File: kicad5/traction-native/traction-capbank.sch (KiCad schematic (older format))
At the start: 26 parts

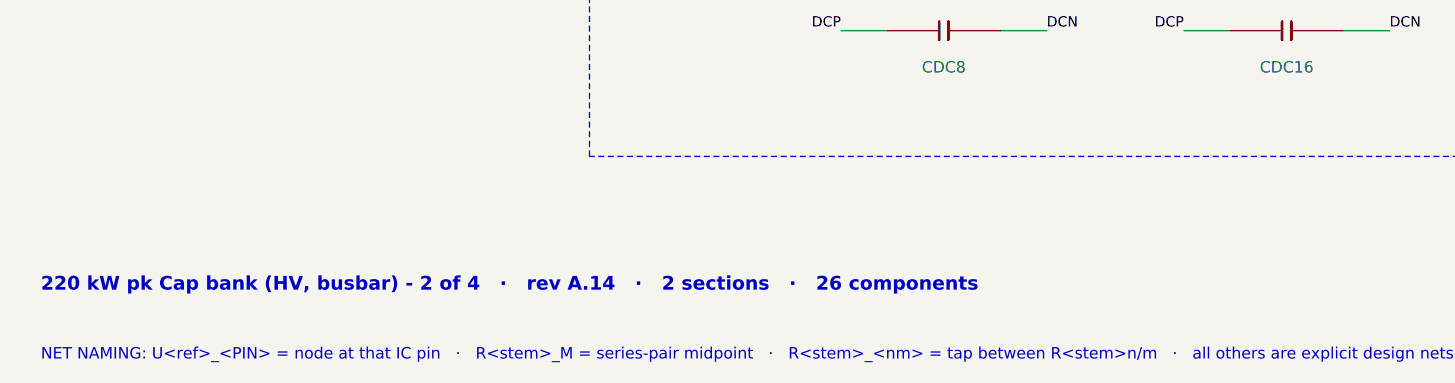
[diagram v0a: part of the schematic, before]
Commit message: Rev A.16: round 17 — gap closure (F174-F189) + round 16 rev A.15 (F167-F173): every gap closed, upgraded or numbered
Round 16 (rev A.15, three rechecks of 32214be): exciter MFB gain 24 k -> 28 k with the amplitude
planes (setpoint 7.2 V pp at the monitor), unidirectional exciter TVS, /33X hold 0.07 A, firmware
acquisition contracts (phase triplets, resolver frame age, coherent SDADC frames); BOM furnished
(spec-class capacitors, drawn-size gate in bom-gen, last placeholders bound with archived sheets).

Round 17 (rev A.16, "close all gaps" / "feel free to upgrade"):
- Hardware: DEXP/DEXN PMEG4050EP-Q rated back-drive diversion (closes the ALM2402 OPEN row);
  exciter TVS -> SMDJ8.5A-HRA (3 kW, AEC-Q101, same pad); fault rows split single fault (PASS
  at any source impedance) vs load-dump-coincident double event; LV entry re-designed as
  LET-THROUGH for ISO 16750-2 test B (TPSMC33A-VR/TPSMC18A-VR anti-series pair at the pin ahead
  of the reverse Schottky, TPSMC33CA-VR on the power board, CLVC3 100 uF hybrid polymer, FLVC
  5 A fuse, DIGN US1M, ULDO15 D2PAK) — pulse 1 was avalanching DREVC, the 2023 26 V jump start
  opened the old TVS, the polyfuse was undersized at 9 V; RFS4 -> ESR18 1206.
- Stale/unsourced rows recomputed: cold-crank excitation, PTC hold (IR-13), discharge resistor
  no-flame statement, hall reference drift, ASC command-path collapse.
- KiCad: a KiCad 9/10 set (kicad/traction, Traction-Inverter-KiCad-modern.zip) proved by
  kicad-cli netlist export on every board with mutation tests; KiCad 10 cannot resolve the KiCad 5
  legacy symbols; the proof exposed harness pins numbered P1-P40 and the SMDJ drawn as a resistor
  in the legacy generator — fixed; sym-lib-table + cache library in both legacy sets.
- Firmware: all 35 open contract items closed (FW-08 zero-current decision, FW-31 liveness,
  FW-32 UDS service-lock routine, FW-33 supply-overvoltage supervision), FS26 watchdog answer
  3.0 ms -> 2.0 ms, ASC-exit release wait CAL, 39-row silicon/RM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
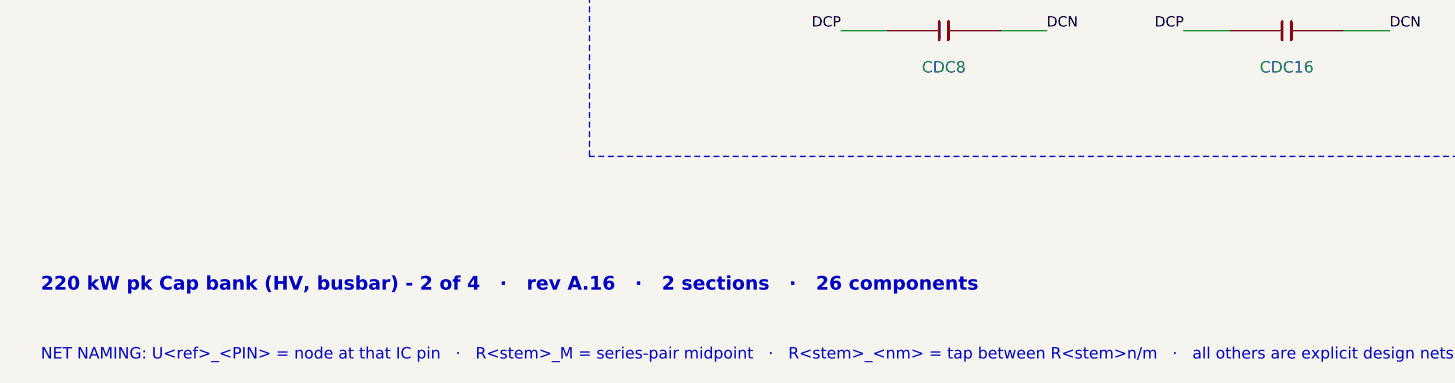
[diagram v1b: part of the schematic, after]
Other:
- note added: "220 kW pk Cap bank (HV, busbar) - 2 of 4 · rev A.16 · 2 sections · 26 components"
- note removed: "220 kW pk Cap bank (HV, busbar) - 2 of 4 · rev A.14 · 2 sections · 26 components"
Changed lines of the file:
@@
 Title "Traction Inverter — Cap bank (busbar assembly, 320 uF)"
 Date "2026-09-23"
-Rev "A.14"
+Rev "A.16"
 Comp "Traction Inverter 220 kW pk - Cap bank (HV, busbar), sheet 2 of 4"
 Comment1 "Inverter = Power board + Cap bank busbar + bolt-on Discharge board (all HV) + Control card (LV); safe state holds with any link lost"
@@
 $EndDescr
 Text Notes 600 5100 0    60   ~ 12
-220 kW pk Cap bank (HV, busbar) - 2 of 4   ·   rev A.14   ·   2 sections   ·   26 components
+220 kW pk Cap bank (HV, busbar) - 2 of 4   ·   rev A.16   ·   2 sections   ·   26 components
 Text Notes 600 5400 0    50   ~ 0
 NET NAMING: U<ref>_<PIN> = node at that IC pin   ·   R<stem>_M = series-pair midpoint   ·   R<stem>_<nm> = tap between R<stem>n/m   ·   all others are explicit design nets   ·   same name on another sheet = same net, joined only at the named connector/stud/tab

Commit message: Rev A.17: round 18 — three rechecks of 4425af9 (F190-F198): diversion diodes on the amplifier node (loop passes RSX), diode cell cathode = pin 1 on all 35 diodes, exciter TVS/PTC rows at worst corners + ECU-asleep sustained short (WARN rows, layout rule, QP-RX-04 2b gate), anti-surge RSX, NCV4276C reverse current = QP-RX-05 gate + VR-33, IR-16/IR-42, firmware FW-34..36 (sample freshness, cadence-locked resolver frames, latency sign) + three self-found instances
Co-Authored-By: Claude Fable 5.1 <noreply@anthropic.com>
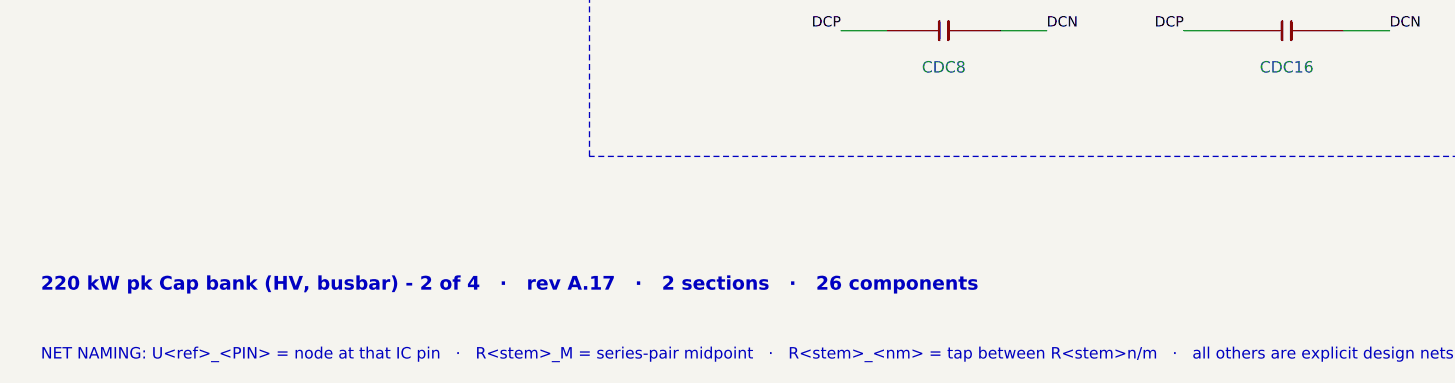
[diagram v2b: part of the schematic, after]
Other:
- note added: "220 kW pk Cap bank (HV, busbar) - 2 of 4 · rev A.17 · 2 sections · 26 components"
- note removed: "220 kW pk Cap bank (HV, busbar) - 2 of 4 · rev A.16 · 2 sections · 26 components"
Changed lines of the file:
@@
 Title "Traction Inverter — Cap bank (busbar assembly, 320 uF)"
 Date "2026-09-23"
-Rev "A.16"
+Rev "A.17"
 Comp "Traction Inverter 220 kW pk - Cap bank (HV, busbar), sheet 2 of 4"
 Comment1 "Inverter = Power board + Cap bank busbar + bolt-on Discharge board (all HV) + Control card (LV); safe state holds with any link lost"
@@
 $EndDescr
 Text Notes 600 5100 0    60   ~ 12
-220 kW pk Cap bank (HV, busbar) - 2 of 4   ·   rev A.16   ·   2 sections   ·   26 components
+220 kW pk Cap bank (HV, busbar) - 2 of 4   ·   rev A.17   ·   2 sections   ·   26 components
 Text Notes 600 5400 0    50   ~ 0
 NET NAMING: U<ref>_<PIN> = node at that IC pin   ·   R<stem>_M = series-pair midpoint   ·   R<stem>_<nm> = tap between R<stem>n/m   ·   all others are explicit design nets   ·   same name on another sheet = same net, joined only at the named connector/stud/tab

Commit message: Rev A.18: round 19 — three rechecks of e315bf1 (F199-F204): PTC-current row at every permitted voltage (IR-16 0.08/0.14/0.37/0.26 Ω), ≥8 A TVS energy an explicit assumption + QP-RX-04 release criterion, window criterion fixed, exciter TVS → SMDJ7.0A-HRA (coupled island holds the 7.0 V class at a parked 12 V battery / the Marine rail), shared exciter-fault model run for the Marine port (QP-MA-11, kit-loom rule), FW-35 rewritten on an SWG-anchored time origin with clock-derived resync and bounded restart
Co-Authored-By: Claude Fable 5.1 <noreply@anthropic.com>
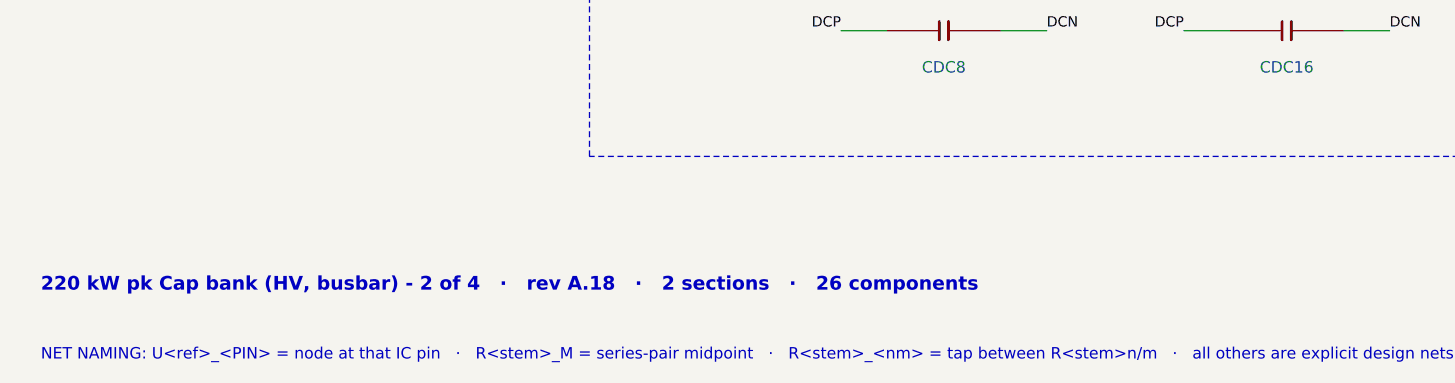
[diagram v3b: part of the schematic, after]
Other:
- note added: "220 kW pk Cap bank (HV, busbar) - 2 of 4 · rev A.18 · 2 sections · 26 components"
- note removed: "220 kW pk Cap bank (HV, busbar) - 2 of 4 · rev A.17 · 2 sections · 26 components"
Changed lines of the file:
@@
 Title "Traction Inverter — Cap bank (busbar assembly, 320 uF)"
 Date "2026-09-23"
-Rev "A.17"
+Rev "A.18"
 Comp "Traction Inverter 220 kW pk - Cap bank (HV, busbar), sheet 2 of 4"
 Comment1 "Inverter = Power board + Cap bank busbar + bolt-on Discharge board (all HV) + Control card (LV); safe state holds with any link lost"
@@
 $EndDescr
 Text Notes 600 5100 0    60   ~ 12
-220 kW pk Cap bank (HV, busbar) - 2 of 4   ·   rev A.17   ·   2 sections   ·   26 components
+220 kW pk Cap bank (HV, busbar) - 2 of 4   ·   rev A.18   ·   2 sections   ·   26 components
 Text Notes 600 5400 0    50   ~ 0
 NET NAMING: U<ref>_<PIN> = node at that IC pin   ·   R<stem>_M = series-pair midpoint   ·   R<stem>_<nm> = tap between R<stem>n/m   ·   all others are explicit design nets   ·   same name on another sheet = same net, joined only at the named connector/stud/tab

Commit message: Rev A.19: round 20 — three rechecks of 00f6252 (F205-F207): TVS alternate to the 7.0 V class + lock, 4XX discharge alternate 470→220 Ω + lock, T-05/T-06 firmware ID, 8.5 V-era figures re-derived at the IR-16 allocations
Co-Authored-By: Claude Fable 5.1 <noreply@anthropic.com>
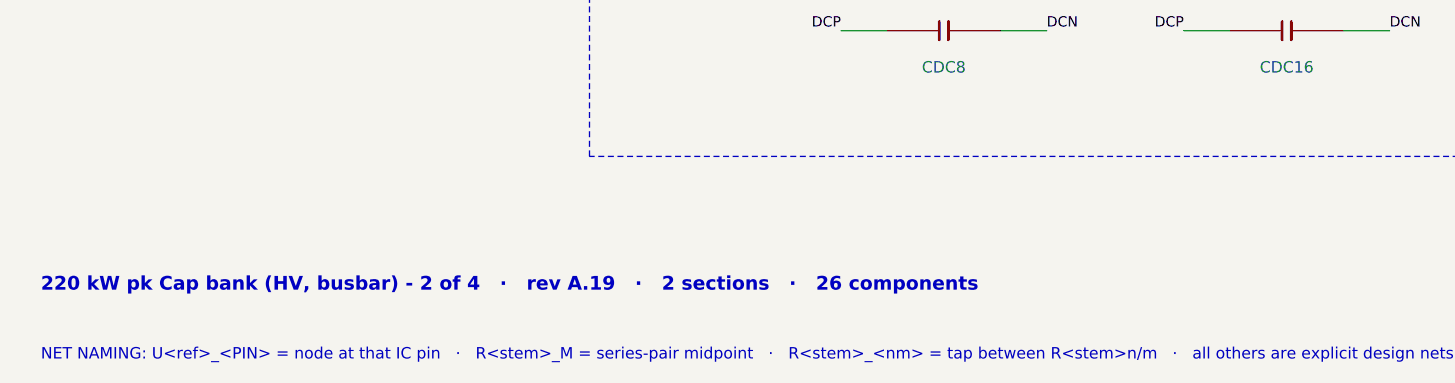
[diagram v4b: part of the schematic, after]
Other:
- note added: "220 kW pk Cap bank (HV, busbar) - 2 of 4 · rev A.19 · 2 sections · 26 components"
- note removed: "220 kW pk Cap bank (HV, busbar) - 2 of 4 · rev A.18 · 2 sections · 26 components"
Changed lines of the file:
@@
 Title "Traction Inverter — Cap bank (busbar assembly, 320 uF)"
 Date "2026-09-23"
-Rev "A.18"
+Rev "A.19"
 Comp "Traction Inverter 220 kW pk - Cap bank (HV, busbar), sheet 2 of 4"
 Comment1 "Inverter = Power board + Cap bank busbar + bolt-on Discharge board (all HV) + Control card (LV); safe state holds with any link lost"
@@
 $EndDescr
 Text Notes 600 5100 0    60   ~ 12
-220 kW pk Cap bank (HV, busbar) - 2 of 4   ·   rev A.18   ·   2 sections   ·   26 components
+220 kW pk Cap bank (HV, busbar) - 2 of 4   ·   rev A.19   ·   2 sections   ·   26 components
 Text Notes 600 5400 0    50   ~ 0
 NET NAMING: U<ref>_<PIN> = node at that IC pin   ·   R<stem>_M = series-pair midpoint   ·   R<stem>_<nm> = tap between R<stem>n/m   ·   all others are explicit design nets   ·   same name on another sheet = same net, joined only at the named connector/stud/tab

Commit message: Rev A.20: round 21 — three rechecks of 551c405 (F208): stale 0.29 Ω in gate ㉘ and the QP-RX-04 fixture instruction → 0.37 Ω, last 8.5 V-era figures aligned, Marine sweep cross-references at the current values
Co-Authored-By: Claude Fable 5.1 <noreply@anthropic.com>
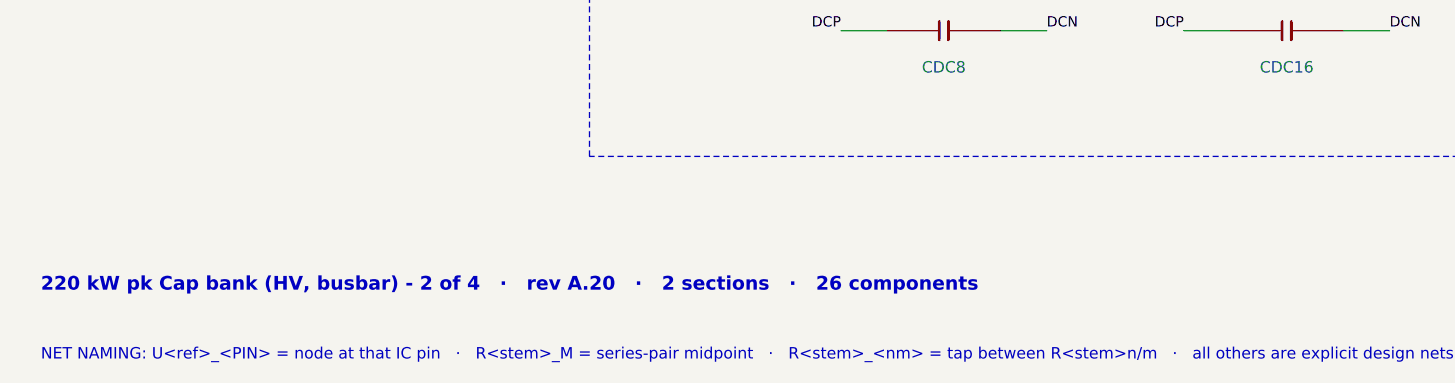
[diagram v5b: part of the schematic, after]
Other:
- note added: "220 kW pk Cap bank (HV, busbar) - 2 of 4 · rev A.20 · 2 sections · 26 components"
- note removed: "220 kW pk Cap bank (HV, busbar) - 2 of 4 · rev A.19 · 2 sections · 26 components"
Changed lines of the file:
@@
 Title "Traction Inverter — Cap bank (busbar assembly, 320 uF)"
 Date "2026-09-23"
-Rev "A.19"
+Rev "A.20"
 Comp "Traction Inverter 220 kW pk - Cap bank (HV, busbar), sheet 2 of 4"
 Comment1 "Inverter = Power board + Cap bank busbar + bolt-on Discharge board (all HV) + Control card (LV); safe state holds with any link lost"
@@
 $EndDescr
 Text Notes 600 5100 0    60   ~ 12
-220 kW pk Cap bank (HV, busbar) - 2 of 4   ·   rev A.19   ·   2 sections   ·   26 components
+220 kW pk Cap bank (HV, busbar) - 2 of 4   ·   rev A.20   ·   2 sections   ·   26 components
 Text Notes 600 5400 0    50   ~ 0
 NET NAMING: U<ref>_<PIN> = node at that IC pin   ·   R<stem>_M = series-pair midpoint   ·   R<stem>_<nm> = tap between R<stem>n/m   ·   all others are explicit design nets   ·   same name on another sheet = same net, joined only at the named connector/stud/tab
